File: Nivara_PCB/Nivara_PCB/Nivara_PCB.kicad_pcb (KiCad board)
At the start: 4 copper layers, 102.2 x 83 mm, 160 parts, among them CN1 ANALOG_IN, CN2 RELAY, J1 AUXILIAR, K1 SRA-24VDC-CL, K2 SRA-24VDC-CL, P1 NPN_IN, P2 PNP_IN, P3 D_IN, P4 RUN/STOP, P5 NPN_OUT, P6 PNP_OUT, P7 RS485, P8 ANALOG_OUT., Q1 IRLML0040, Q2 AO3407A, Q3 IRLML0040, Q4 AO3407A, Q5 IRLML6402TRPBF-JSM, SW1 SKRPACE010, SW2 SKRPACE010, U1 2.54-2*2, U10 GP8201S-TC50-EW, U11 LK1802, U12 LTV-357T, U13 LTV-357T, U14 LTV-357T, U15 LTV-357T, U16 LTV-357T, U17 LTV-357T, U18 LTV-357T, U19 GP8303-TC50-EW, U2 FUENTE IN, U3 ESP32-S3-WROOM-1, U4 AP63200WU, U5 RSM3485ECHT_C2992406, U6 LTV-357T, U7 LTV-357T, U8 LTV-357T, U9 LTV-357T

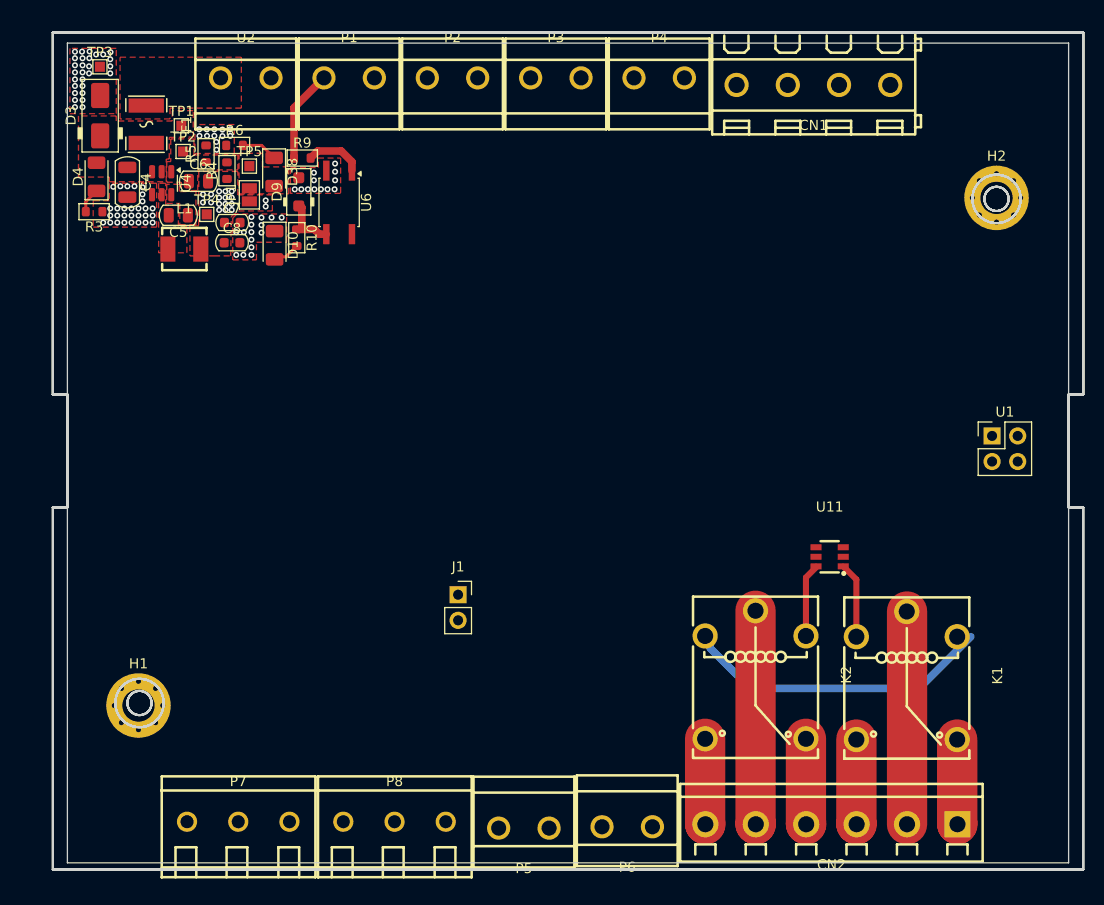
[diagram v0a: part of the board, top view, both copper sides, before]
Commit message: Cambio en las dimensiones de la PCB y actualización de archivos relacionados.
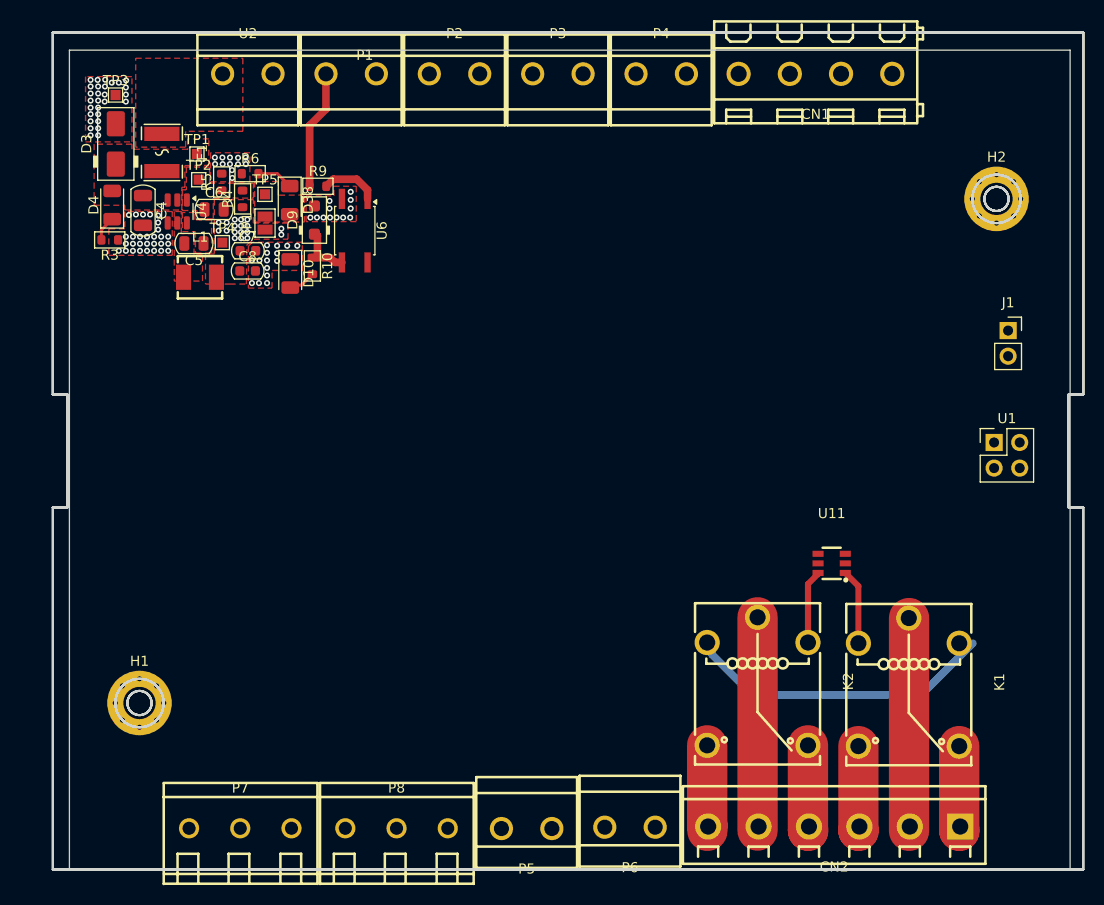
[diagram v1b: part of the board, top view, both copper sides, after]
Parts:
- moved J1 60.5 mm to (260.6, 69.2)
- moved C5 3.20 mm to (179.8, 60.6)
- moved C6 3.20 mm to (181.8, 57.2)
- moved D3 3.20 mm to (172.1, 50.7)
- moved D38 3.20 mm to (189.3, 56.3)
- moved R5 3.20 mm to (182.6, 54.5)
- moved TP3 3.20 mm to (172.0, 45.9)
- moved TP4 3.20 mm to (182.6, 60.5)
- moved C7 3.20 mm to (185.2, 61.3)
- moved D4 3.20 mm to (171.7, 56.8)
- moved D9 3.20 mm to (191.7, 58.2)
- moved L1 3.20 mm to (180.4, 63.9)
- moved TP2 3.20 mm to (180.3, 54.2)
- moved U4 3.20 mm to (178.2, 57.4)
- moved U6 3.20 mm to (195.7, 59.3)
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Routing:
- net /NIVARA_BOARD/NPN_IN_1: track 9.18 -> 11.8 mm
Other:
- outline, holes or cut-outs redrawn

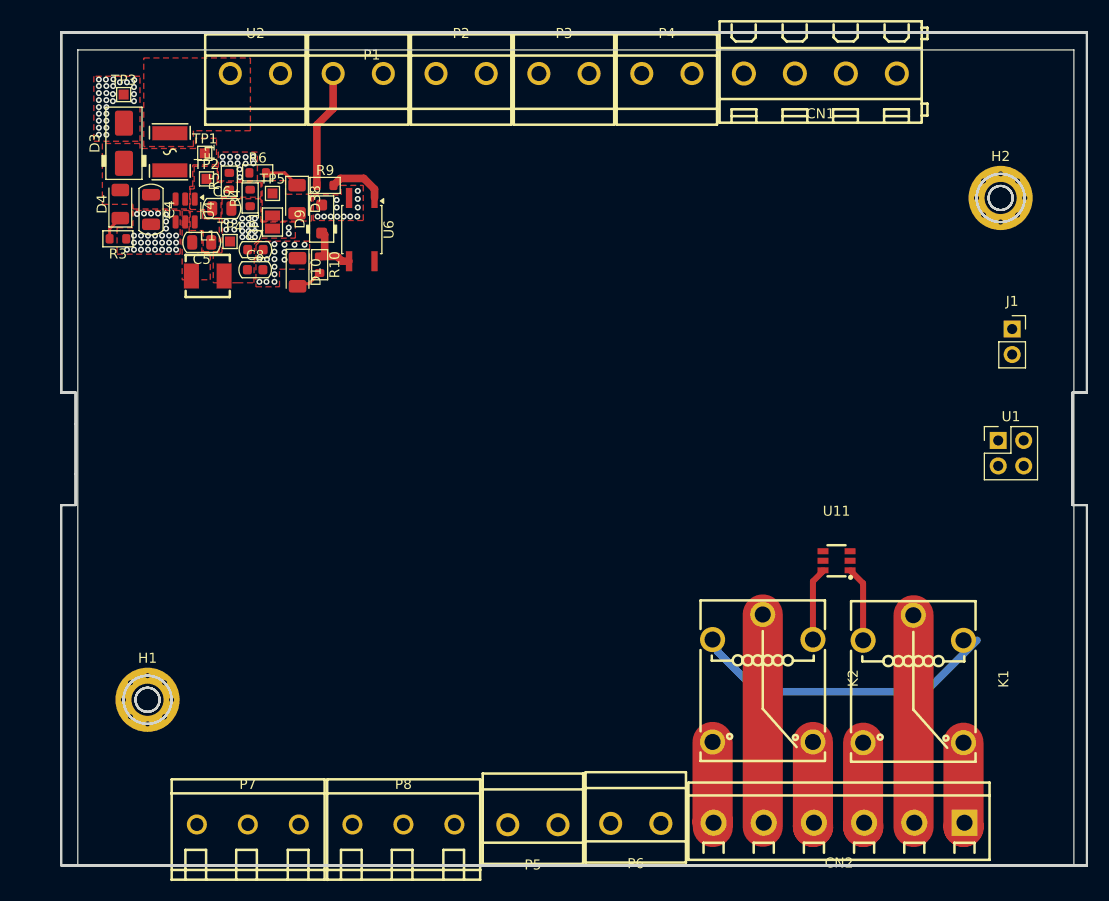
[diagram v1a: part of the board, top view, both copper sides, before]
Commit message: Cambios en dimensiones de nivara PCB
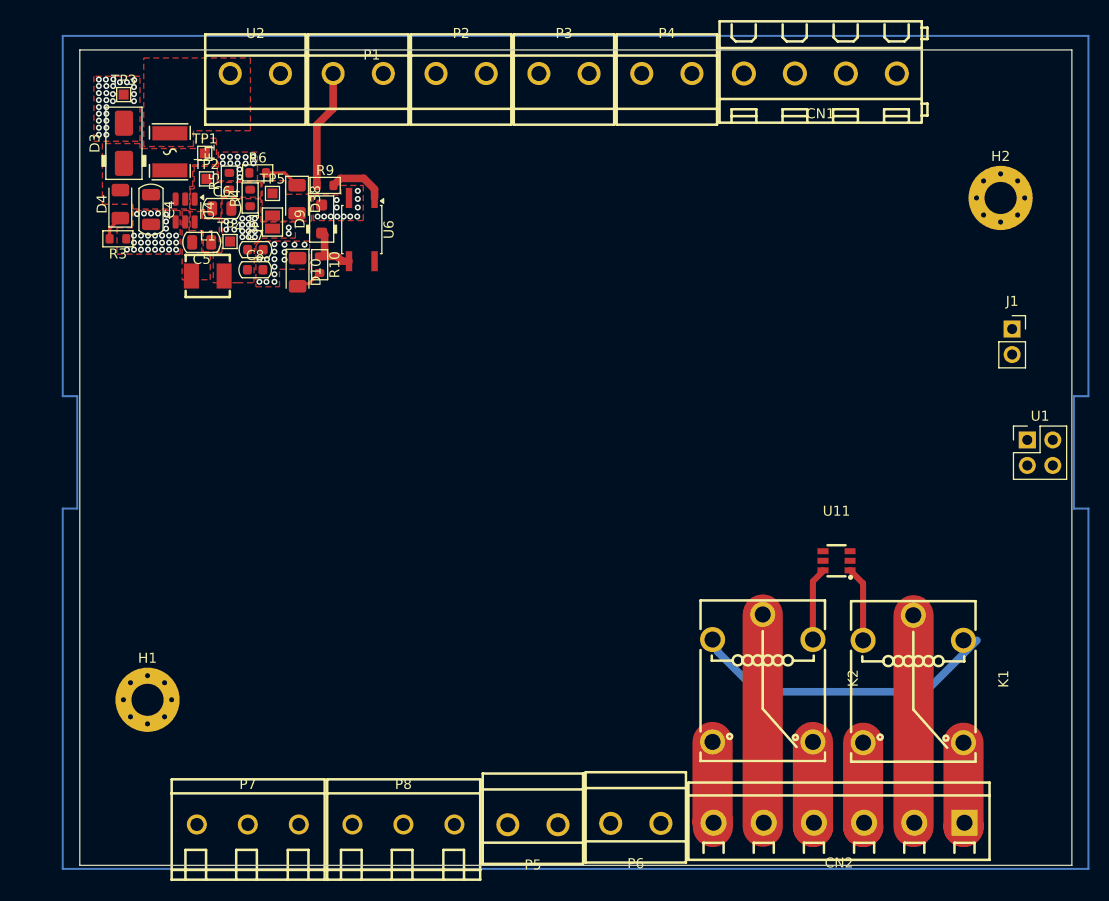
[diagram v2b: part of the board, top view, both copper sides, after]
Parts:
- moved U1 2.90 mm to (262.1, 80.3)
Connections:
- U1 pad 1: Net-(D1-A) -> /NIVARA_BOARD/USB_D-
- U1 pad 2: /NIVARA_BOARD/USB_D+ -> GND
- U1 pad 3: GND -> /NIVARA_BOARD/USB_D+
- U1 pad 4: /NIVARA_BOARD/USB_D- -> Net-(D1-A)
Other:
- board size 102.2 x 83 mm -> 98.8 x 81.2 mm

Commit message: Cambios en el diseño del pcb.
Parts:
- moved D24 94.8 mm to (178.6, 22.9)
- moved R34 94.8 mm to (183.5, 24.9)
- moved U14 94.8 mm to (180.7, 18.3)
- moved D11 94.8 mm to (178.6, 26.6)
- moved R33 94.8 mm to (183.5, 22.2)
- moved C10 5.71 mm to (120.5, 109.2)
- moved C13 5.71 mm to (75.9, 85.6)
- moved C14 5.71 mm to (135.3, 111.5)
- moved C15 5.71 mm to (67.6, 123.0)
- moved C16 5.71 mm to (79.5, 123.0)
- moved C2 5.71 mm to (88.3, 55.9)
- moved C3 5.71 mm to (88.3, 58.6)
- moved C9 5.71 mm to (115.5, 50.5)
- moved D1 5.71 mm to (131.6, 77.1)
- moved D13 5.71 mm to (99.5, 101.3)
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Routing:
- net /NIVARA_BOARD/RLY_2_NO: track 8.49 -> 7.56 mm
- net /NIVARA_BOARD/RLY_2_NC: track 8.49 -> 7.56 mm
- net /NIVARA_BOARD/RLY_1_NO: track 8.41 -> 7.48 mm
- net /NIVARA_BOARD/RLY_1_NC: track 8.41 -> 7.48 mm
- net /NIVARA_BOARD/RLY_1_C: track 21.1 -> 20.2 mm
- net /NIVARA_BOARD/RLY_2_C: track 21.1 -> 20.3 mm

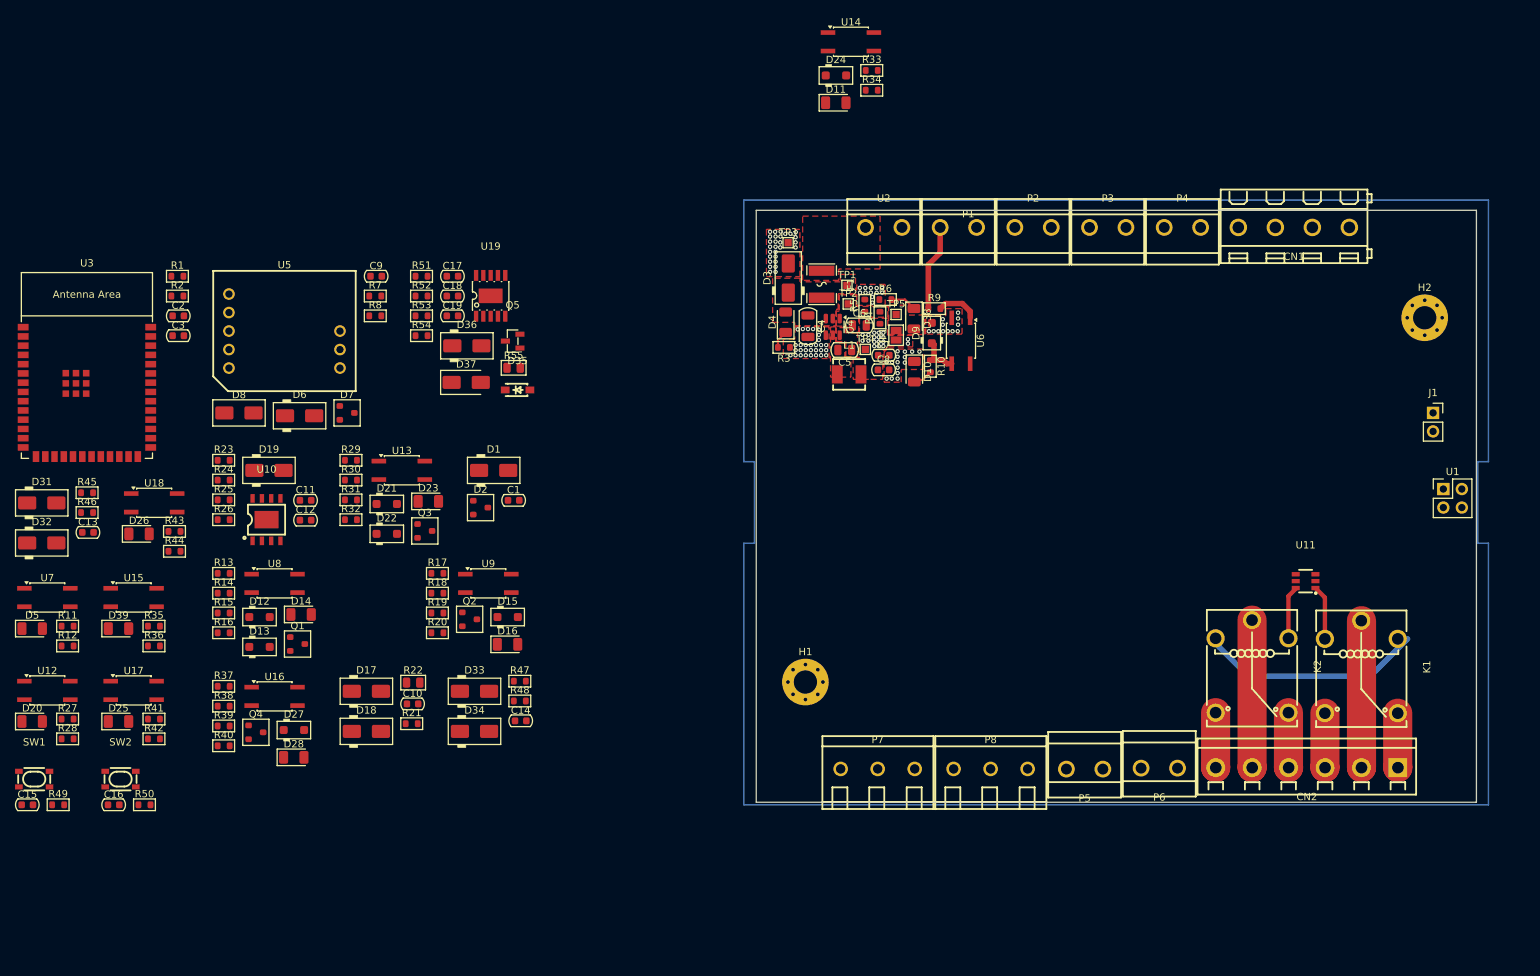
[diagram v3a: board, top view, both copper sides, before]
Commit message: Devolviendo los archivos eliminados sin querer a git.
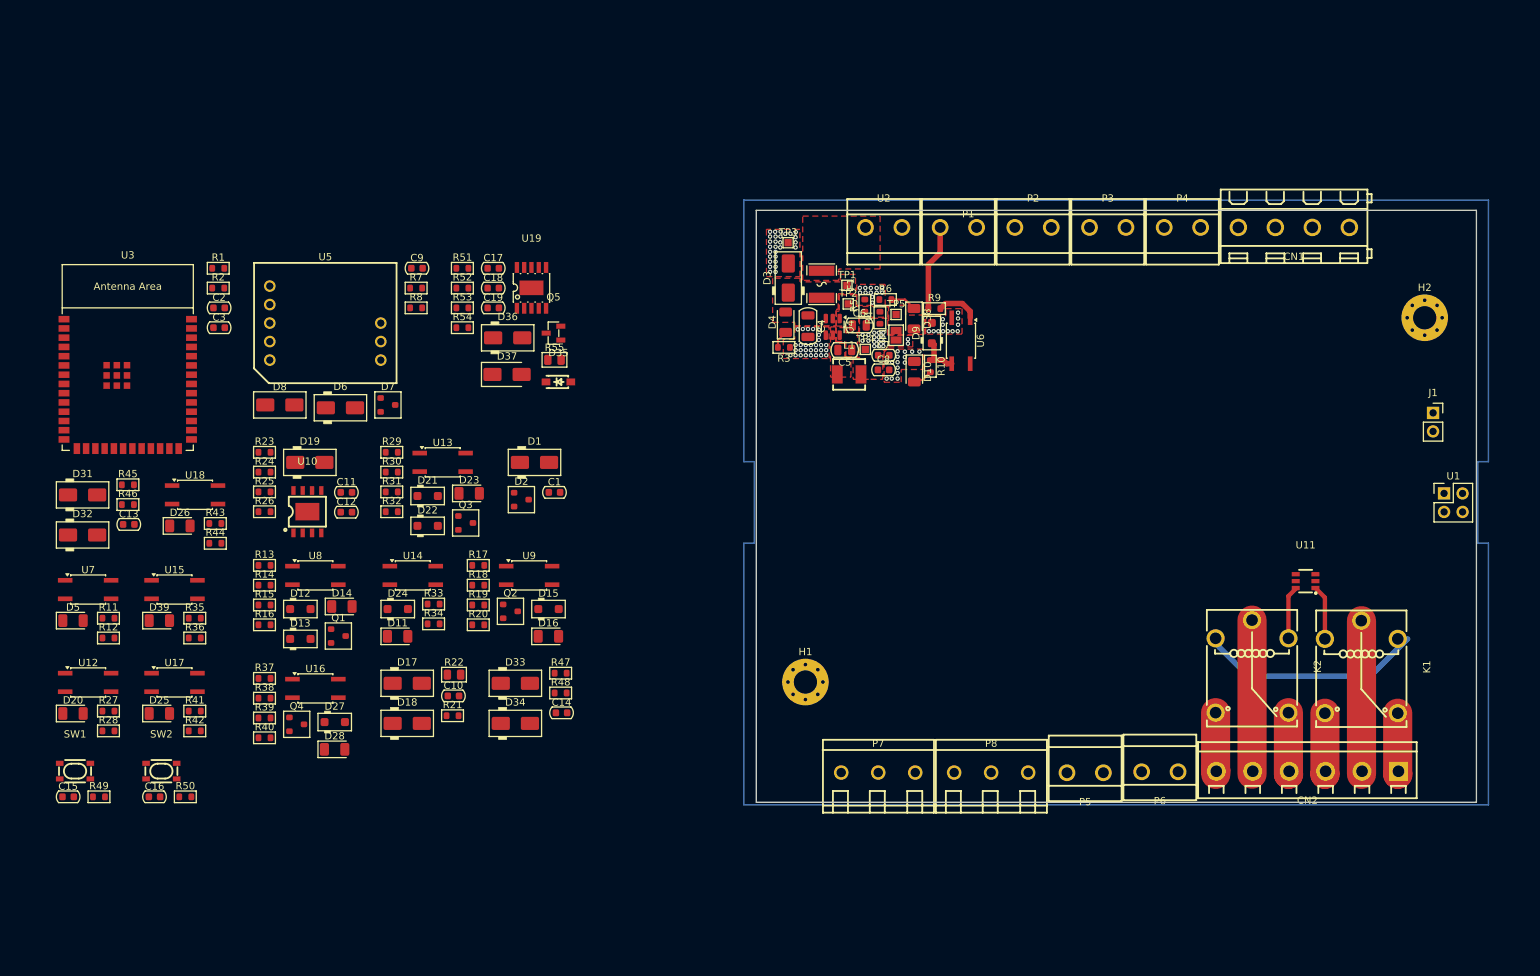
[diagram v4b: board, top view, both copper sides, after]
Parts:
- moved D24 94.8 mm to (118.4, 96.1)
- moved R34 94.8 mm to (123.4, 98.2)
- moved U14 94.8 mm to (120.5, 91.5)
- moved D11 94.8 mm to (118.4, 99.9)
- moved R33 94.8 mm to (123.4, 95.4)
- moved C10 5.71 mm to (126.1, 108.1)
- moved C13 5.71 mm to (81.5, 84.5)
- moved C14 5.71 mm to (140.9, 110.4)
- moved C15 5.71 mm to (73.2, 121.9)
- moved C16 5.71 mm to (85.1, 121.9)
- moved C2 5.71 mm to (93.9, 54.8)
- moved C3 5.71 mm to (93.9, 57.5)
- moved C9 5.71 mm to (121.1, 49.4)
- moved D1 5.71 mm to (137.2, 76.0)
- moved D13 5.71 mm to (105.1, 100.2)
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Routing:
- net /NIVARA_BOARD/RLY_2_NO: track 7.56 -> 8.49 mm
- net /NIVARA_BOARD/RLY_2_NC: track 7.56 -> 8.49 mm
- net /NIVARA_BOARD/RLY_1_NO: track 7.48 -> 8.41 mm
- net /NIVARA_BOARD/RLY_1_NC: track 7.48 -> 8.41 mm
- net /NIVARA_BOARD/RLY_1_C: track 20.2 -> 21.1 mm
- net /NIVARA_BOARD/RLY_2_C: track 20.3 -> 21.1 mm

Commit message: Guardado los cambios con una sola fuente.
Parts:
- added R56: 33, PCM_Resistor_SMD_AKL:R_0603_1608Metric, F.Cu at (258.2, 82.8)
- added R57: 33, PCM_Resistor_SMD_AKL:R_0603_1608Metric, F.Cu at (258.1, 80.3)
- R1, R2: value 220 -> 33
- U1: footprint Connector_PinHeader_2.54mm:PinHeader_2x02_P2.54mm_Vertical -> Connector_PinSocket_2.54mm:PinSocket_2x02_P2.54mm_Vertical
- U3: footprint PCM_Espressif:ESP32-S3-WROOM-1 -> RF_Module:ESP32-S3-WROOM-1
- moved U3 181.8 mm to (260.0, 98.8), turned to -90 degrees
- moved D32 178.3 mm to (251.3, 57.9), turned to 180 degrees
- moved D31 178.1 mm to (251.3, 53.5)
- moved R45 172.3 mm to (251.3, 50.4), turned to 180 degrees
- moved C13 171.4 mm to (251.3, 61.1), turned to 180 degrees
- moved R46 170.9 mm to (251.3, 63.2)
- moved D20 148.3 mm to (214.1, 62.1), turned to 180 degrees
- moved R27 147.6 mm to (213.6, 50.3)
- moved U12 146.8 mm to (213.9, 56.1), turned to -90 degrees
- moved R28 142.3 mm to (212.8, 65.2), turned to 90 degrees
- moved R41 142.2 mm to (219.5, 50.2)
- moved D25 142.0 mm to (219.2, 62.1), turned to 180 degrees
- moved U17 140.5 mm to (219.0, 56.0), turned to -90 degrees
- moved D26 139.1 mm to (225.7, 61.7), turned to 180 degrees
- moved U18 137.2 mm to (225.6, 55.9), turned to -90 degrees
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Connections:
- net /NIVARA_BOARD/A_0-32_IN/A_OUT renamed /NIVARA_BOARD/A_0-32_IN/A_V_OUT
- D2 pad 1: /NIVARA_BOARD/USB_D+ -> /D+
- D2 pad 2: /NIVARA_BOARD/USB_D- -> /D-
- R47 pad 2: /NIVARA_BOARD/A_0-10_IN/A_V_IN -> /NIVARA_BOARD/A0_10_IN_1
- U1 pad 1: /NIVARA_BOARD/USB_D- -> GND
- U1 pad 2: GND -> /D-
- U1 pad 3: /NIVARA_BOARD/USB_D+ -> Net-(D1-A)
- U1 pad 4: Net-(D1-A) -> /D+
- U3 pad 13: /NIVARA_BOARD/USB_D- -> /NIVARA_BOARD/USB_D+
- U3 pad 14: /NIVARA_BOARD/USB_D+ -> /NIVARA_BOARD/USB_D-
- U3 pad 6: /NIVARA_BOARD/A_OUT -> /NIVARA_BOARD/A_0-10_IN/A_V_OUT
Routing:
- net VCC: track 30.8 -> 205.1 mm, vias 0 -> 24
- net /NIVARA_BOARD/USB_D-: track 0.00 -> 13.3 mm
- net /NIVARA_BOARD/USB_D+: track 0.00 -> 11.8 mm
- net /NIVARA_BOARD/PNP_IN_2: track 0.00 -> 9.90 mm
- net /NIVARA_BOARD/A4_20_IN_1: track 0.00 -> 9.50 mm
- net /NIVARA_BOARD/PNP_IN_1: track 0.00 -> 9.10 mm
- net /NIVARA_BOARD/A0_32_IN_1: track 0.00 -> 8.91 mm
- net /NIVARA_BOARD/A0_10_IN_1: track 0.00 -> 7.39 mm
- net /NIVARA_BOARD/RUN/STOP: track 0.00 -> 6.87 mm
- net /NIVARA_BOARD/D_IN_1: track 0.00 -> 6.75 mm
- net /NIVARA_BOARD/D_IN_2: track 0.00 -> 6.58 mm
- net /NIVARA_BOARD/NPN_IN_2: track 0.00 -> 6.53 mm
- net /NIVARA_BOARD/NPN_IN_2/NPN_OUT: track 0.00 -> 5.30 mm
- net /NIVARA_BOARD/NPN_IN_1: track 11.8 -> 6.97 mm
- net /D+: track 0.00 -> 4.39 mm
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- added copper zone on In2.Cu, net +3.3V
- added copper zone on F.Cu, net /NIVARA_BOARD/4-20mA_IN/ESP_4-20_IN
- added copper zone on F.Cu, net /NIVARA_BOARD/A_0-10_IN/A_V_OUT
- added copper zone on F.Cu, net /NIVARA_BOARD/A_0-32_IN/A_V_OUT
- added copper zone on B.Cu, net GND
- added copper zone on B.Cu, net VCC
